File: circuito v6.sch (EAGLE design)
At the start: 64 parts, among them IC1 LM324N

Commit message: última v6 del día
Creo que no tiene modificaciones salvo que intenté hacer el mapeo para la simulación. Todo lo demás debería estar igual. Se guarda por las dudas.
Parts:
- IC1: SPICEPREFIX B -> X
- LED1, LED2: SPICEMODEL (none) -> DMOD

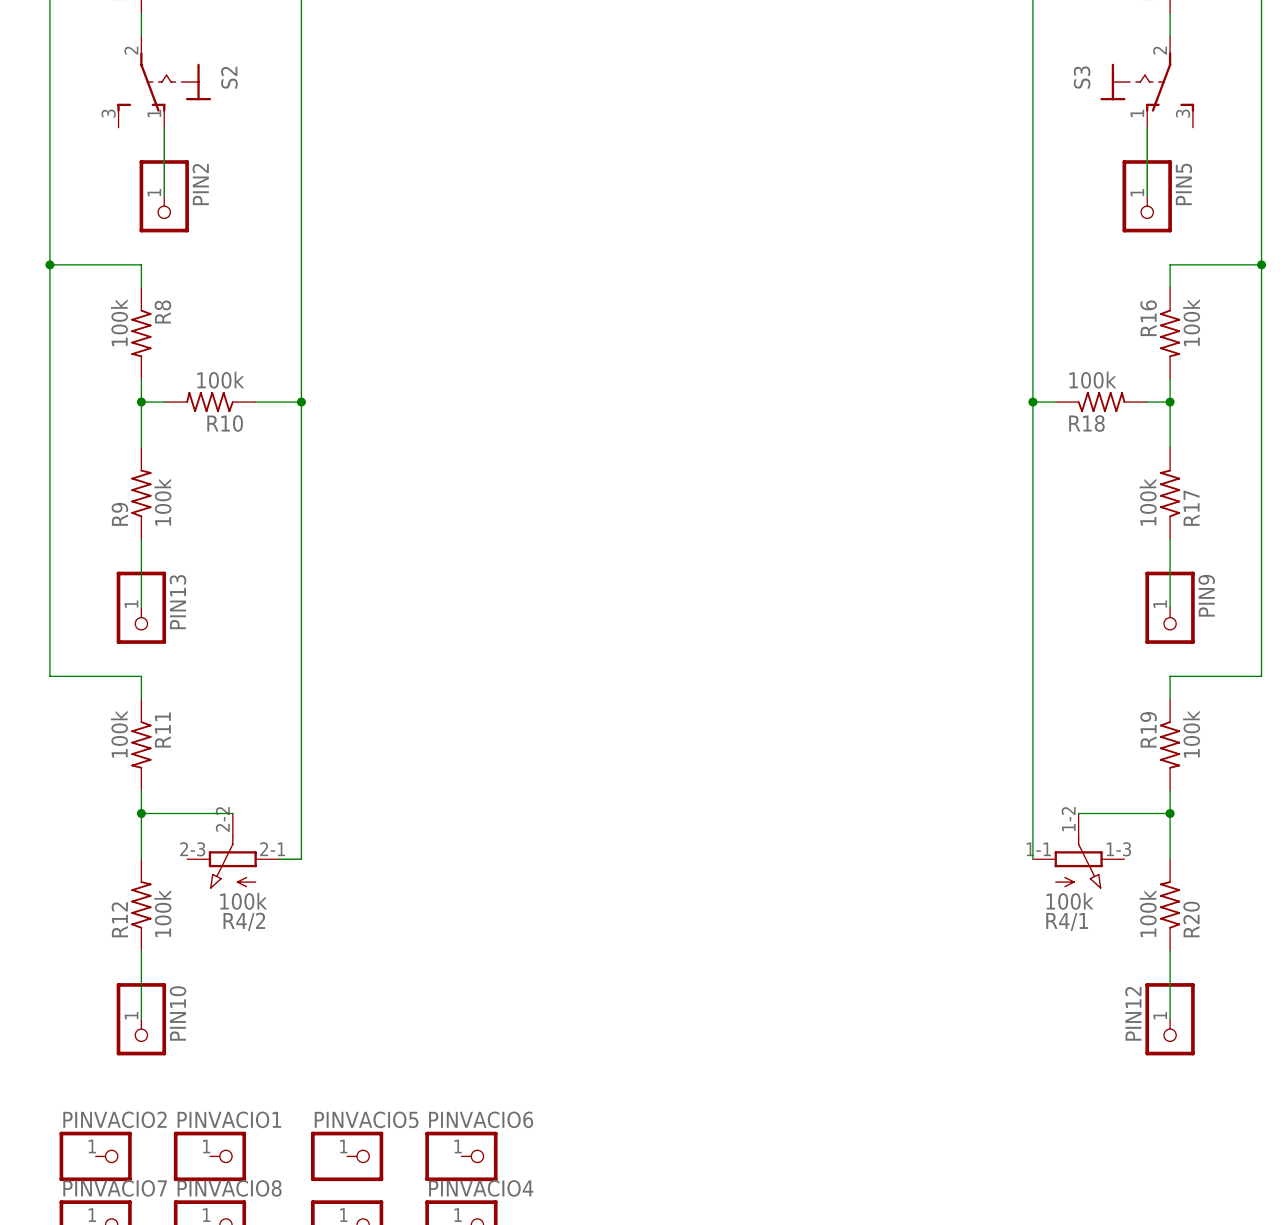
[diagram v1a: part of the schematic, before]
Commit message: Chequeo de lado izq y der de phones
Chequeo de lado izq y der de phones. Cambio nombre de los pines de cada parte en base a eso.
Uso:
Estimulo Izq PIN 11
Estimulo Der PIN 12
Feedback Izq PIN 2
Feedback Der PIN 5
Ruido blanco Izq PIN 9
RUido blanco Der PIN 10

Se agregan ademas cuadritos que clasifican esas partes del circuito.
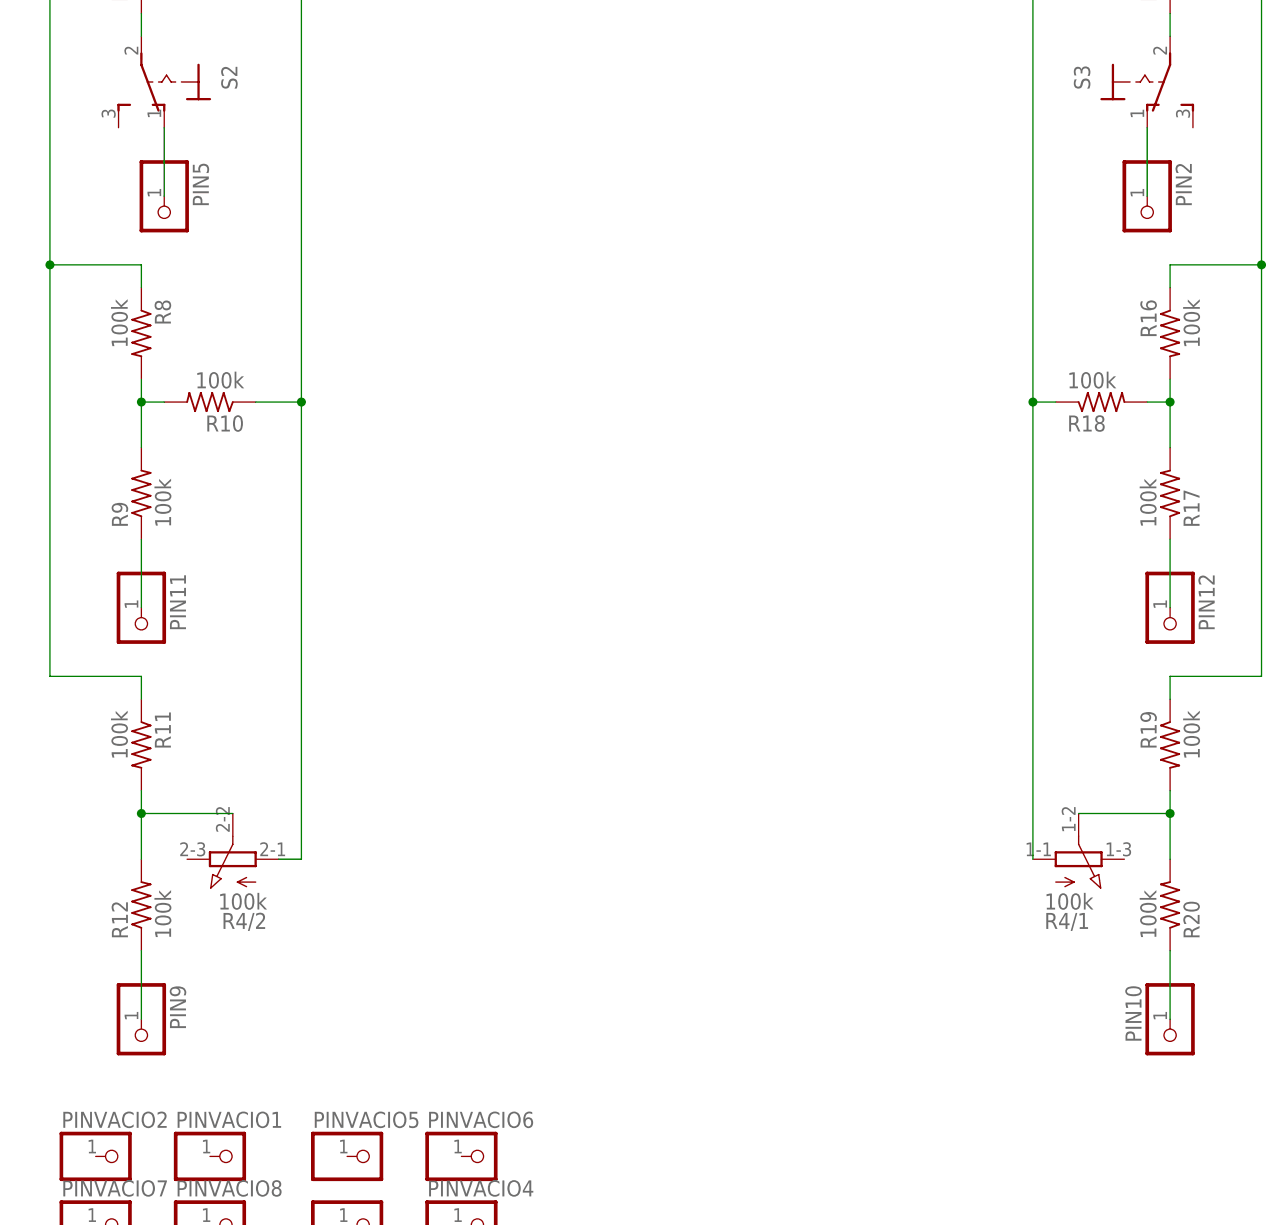
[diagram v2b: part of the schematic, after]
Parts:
- renumbered PIN13 to PIN11
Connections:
- net N$12: now also PIN9.1; no longer PIN10.1
- net N$16: now also PIN2.1; no longer PIN5.1
- net N$20: now also PIN12.1; no longer PIN9.1
- net N$21: now also PIN10.1; no longer PIN12.1
- net N$7: now also PIN5.1; no longer PIN2.1
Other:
- note added: "Estimulo"
- note added: "Feedback con switch"
- note added: "Ruido blanco"
- moved on the sheet: PIN10, PIN12, PIN2, PIN5, PIN9

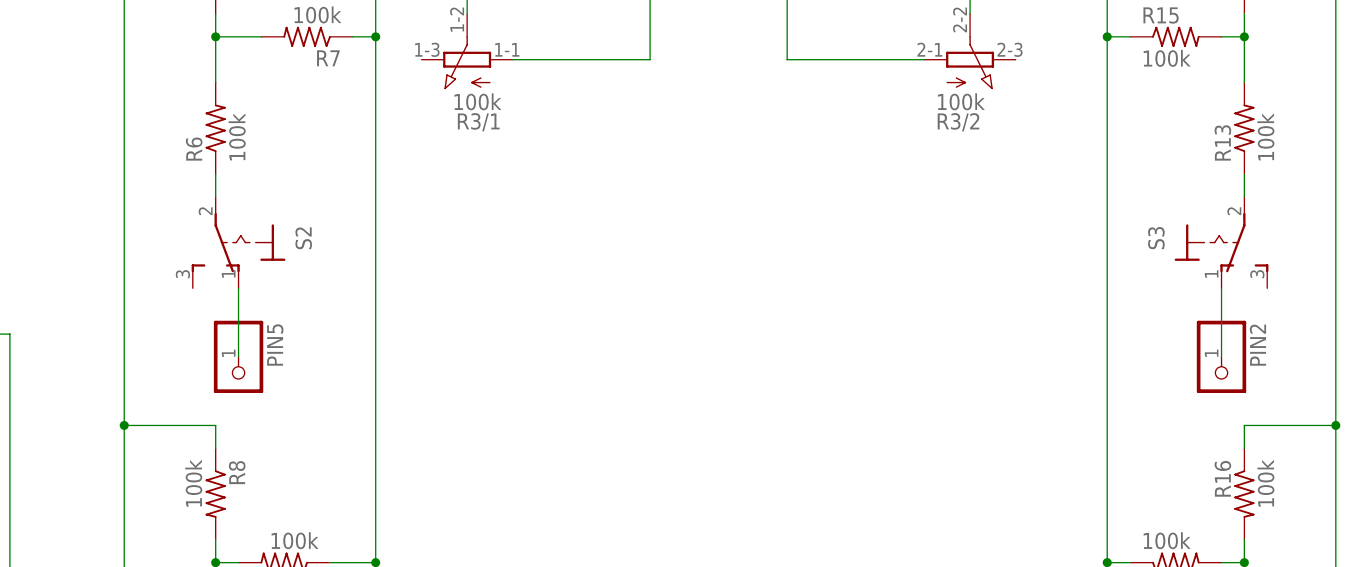
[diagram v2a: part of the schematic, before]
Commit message: Cambio 2 switchs simples por 1 doble
Los switches simples que se van son los que controlan el feedback
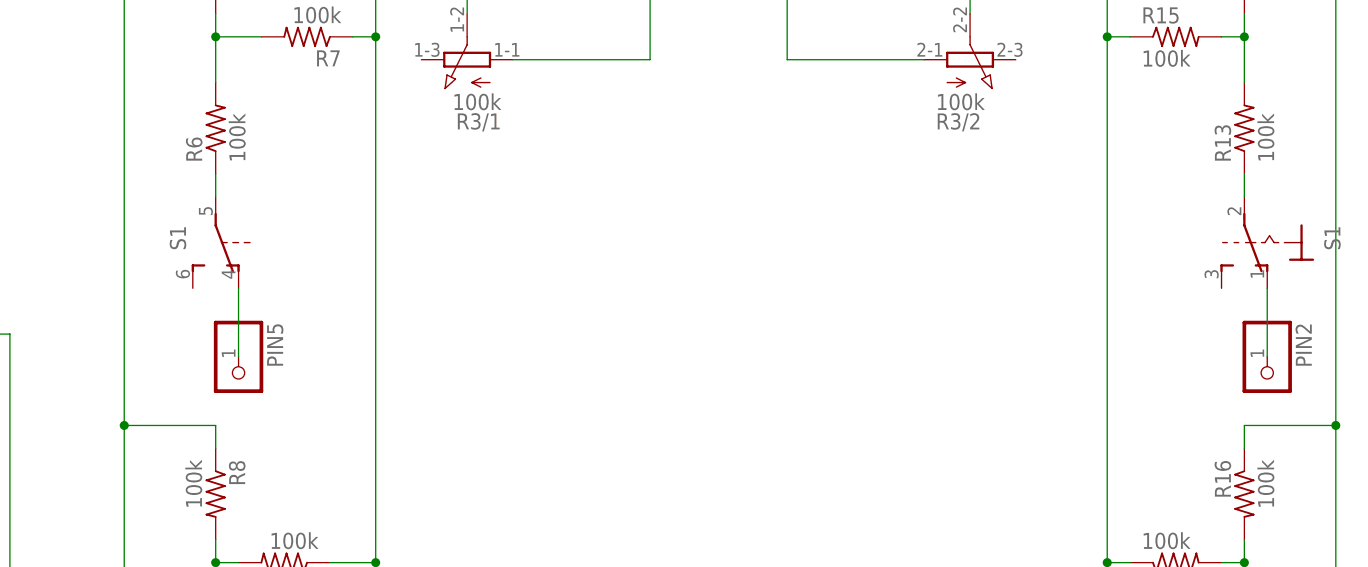
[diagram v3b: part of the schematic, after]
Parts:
- removed S2, S3: (no value), switch:320-916
- added S1: (no value), switch:320-938
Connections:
- removed net N$16: PIN2.1, S3.O
- new net N$10: R13.1, S11.P
- net N$15: now also PIN2.1, S11.O; no longer R13.1, S3.P
- net N$6: now also S1B.P; no longer S2.P
- net N$7: now also S1B.O; no longer S2.O
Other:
- moved on the sheet: PIN2
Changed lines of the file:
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@@
 <attribute name="SPICEPREFIX" value="X"/>
 </part>
-<part name="S2" library="switch" library_urn="urn:adsk.eagle:library:380" deviceset="320-916" device="" package3d_urn="urn:adsk.eagle:package:27678/1">
-<attribute name="SPICEPREFIX" value="J"/>
-</part>
-<part name="S3" library="switch" library_urn="urn:adsk.eagle:library:380" deviceset="320-916" device="" package3d_urn="urn:adsk.eagle:package:27678/1">
-<attribute name="SPICEPREFIX" value="J"/>
-</part>
+<part name="S1" library="switch" library_urn="urn:adsk.eagle:library:380" deviceset="320-938" device="" package3d_urn="urn:adsk.eagle:package:27685/1"/>
 </parts>
 <sheets>
@@
 <attribute name="VALUE" x="87.63" y="6.858" size="1.778" layer="96"/>
 </instance>
-<instance part="PIN2" gate="G$1" x="96.52" y="-27.94" smashed="yes" rot="R270">
-<attribute name="NAME" x="99.695" y="-21.59" size="1.778" layer="95" rot="R270"/>
-<attribute name="VALUE" x="91.44" y="-21.59" size="1.778" layer="96" rot="R270"/>
+<instance part="PIN2" gate="G$1" x="101.6" y="-27.94" smashed="yes" rot="R270">
+<attribute name="NAME" x="104.775" y="-21.59" size="1.778" layer="95" rot="R270"/>
+<attribute name="VALUE" x="96.52" y="-21.59" size="1.778" layer="96" rot="R270"/>
 </instance>
 <instance part="R16" gate="G$1" x="99.06" y="-40.64" smashed="yes" rot="MR270">
@@
 <attribute name="VALUE" x="-11.43" y="-144.78" size="1.778" layer="96"/>
 </instance>
-<instance part="S2" gate="1" x="-12.7" y="-12.7" smashed="yes" rot="R180">
-<attribute name="NAME" x="-6.35" y="-10.795" size="1.778" layer="95" rot="R270"/>
-<attribute name="VALUE" x="-8.89" y="-15.24" size="1.778" layer="96" rot="R270"/>
-</instance>
-<instance part="S3" gate="1" x="96.52" y="-12.7" smashed="yes" rot="MR180">
-<attribute name="NAME" x="90.17" y="-10.795" size="1.778" layer="95" rot="MR270"/>
-<attribute name="VALUE" x="92.71" y="-15.24" size="1.778" layer="96" rot="MR270"/>
+<instance part="S1" gate="B" x="-15.24" y="-12.7" smashed="yes" rot="R180">
+<attribute name="PART" x="-20.32" y="-10.795" size="1.778" layer="95" rot="R270"/>
+</instance>
+<instance part="S1" gate="1" x="101.6" y="-12.7" smashed="yes" rot="R180">
+<attribute name="VALUE" x="105.41" y="-15.24" size="1.778" layer="96" rot="R270"/>
+<attribute name="PART" x="107.95" y="-10.795" size="1.778" layer="95" rot="R270"/>
 </instance>
 </instances>
@@
 </segment>
 </net>
-<net name="N$6" class="0">
-<segment>
-<pinref part="R6" gate="G$1" pin="1"/>
-<wire x1="-15.24" y1="-7.62" x2="-15.24" y2="-5.08" width="0.1524" layer="91"/>
-<pinref part="S2" gate="1" pin="P"/>
-</segment>
-</net>
-<net name="N$7" class="0">
-<segment>
-<pinref part="PIN5" gate="G$1" pin="1"/>
-<wire x1="-12.7" y1="-17.78" x2="-12.7" y2="-25.4" width="0.1524" layer="91"/>
-<pinref part="S2" gate="1" pin="O"/>
-</segment>
-</net>
 <net name="N$9" class="0">
 <segment>
@@
 <wire x1="96.52" y1="10.16" x2="99.06" y2="10.16" width="0.1524" layer="91"/>
 <junction x="99.06" y="10.16"/>
-</segment>
-</net>
-<net name="N$15" class="0">
-<segment>
-<pinref part="R13" gate="G$1" pin="1"/>
-<wire x1="99.06" y1="-5.08" x2="99.06" y2="-7.62" width="0.1524" layer="91"/>
-<pinref part="S3" gate="1" pin="P"/>
-</segment>
-</net>
-<net name="N$16" class="0">
-<segment>
-<pinref part="PIN2" gate="G$1" pin="1"/>
-<wire x1="96.52" y1="-17.78" x2="96.52" y2="-25.4" width="0.1524" layer="91"/>
-<pinref part="S3" gate="1" pin="O"/>
 </segment>
 </net>
@@
 </segment>
 </net>
+<net name="N$6" class="0">
+<segment>
+<pinref part="R6" gate="G$1" pin="1"/>
+<pinref part="S1" gate="B" pin="P"/>
+<wire x1="-15.24" y1="-5.08" x2="-15.24" y2="-7.62" width="0.1524" layer="91"/>
+</segment>
+</net>
+<net name="N$7" class="0">
+<segment>
+<pinref part="S1" gate="B" pin="O"/>
+<pinref part="PIN5" gate="G$1" pin="1"/>
+<wire x1="-12.7" y1="-17.78" x2="-12.7" y2="-25.4" width="0.1524" layer="91"/>
+</segment>
+</net>
+<net name="N$10" class="0">
+<segment>
+<pinref part="S1" gate="1" pin="P"/>
+<pinref part="R13" gate="G$1" pin="1"/>
+<wire x1="99.06" y1="-7.62" x2="99.06" y2="-5.08" width="0.1524" layer="91"/>
+</segment>
+</net>
+<net name="N$15" class="0">
+<segment>
+<pinref part="S1" gate="1" pin="O"/>
+<pinref part="PIN2" gate="G$1" pin="1"/>
+<wire x1="101.6" y1="-17.78" x2="101.6" y2="-25.4" width="0.1524" layer="91"/>
+</segment>
+</net>
